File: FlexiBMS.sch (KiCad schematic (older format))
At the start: 6 parts, among them J1 Conn_02x08_Odd_Even, J7 Conn_01x03

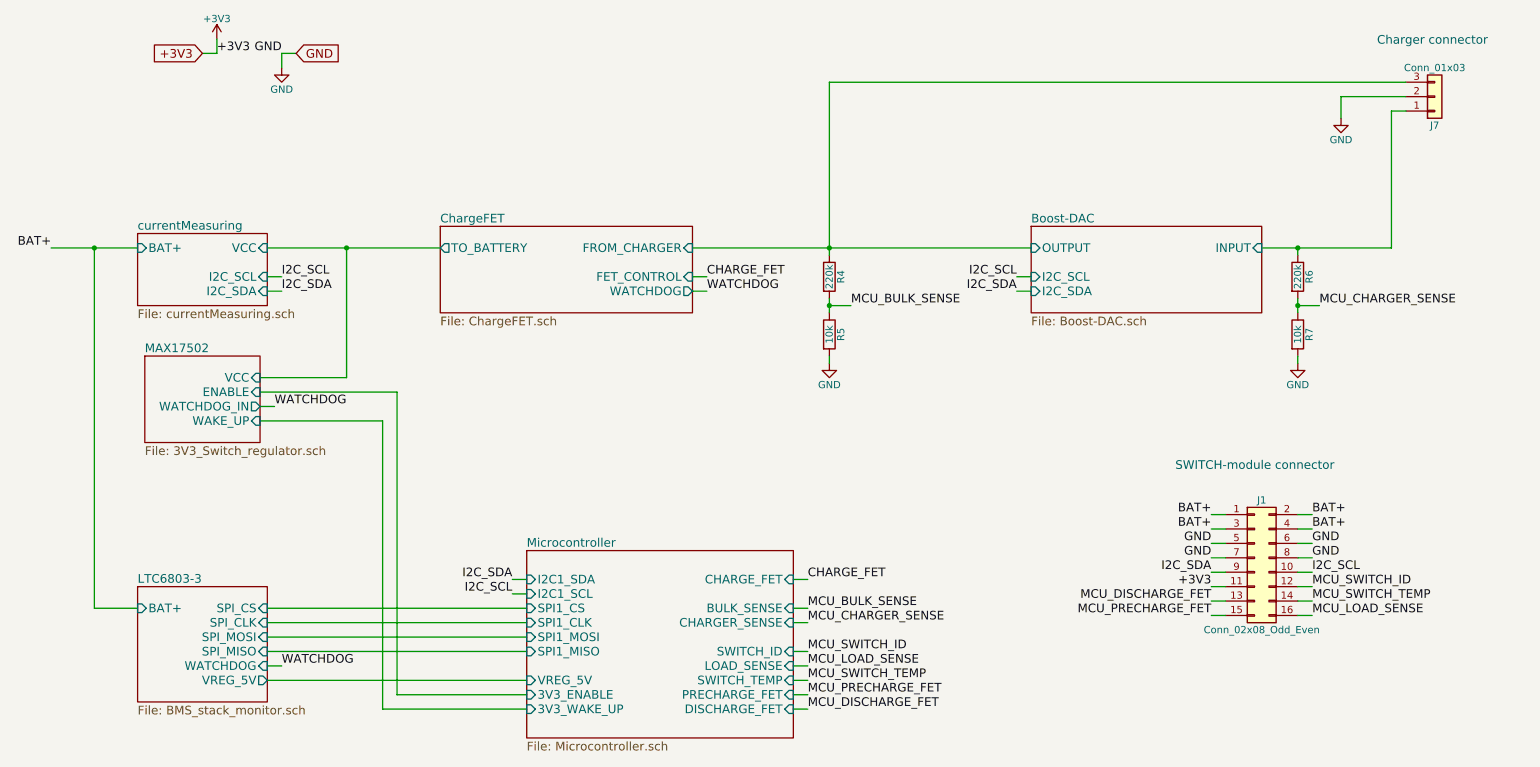
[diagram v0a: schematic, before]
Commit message: HW 0.2 finalized schematic and pcb files, BOM needs to be checked
Lots of major and little problems fixed found in the 0.1

Major changes:
-LTC6803-3 footprint changed to it's correct one
-Boost converter layout and capacitor optimization
-MCU switched from STM32F070CBT6 to ultra low power STM32L433CCT6 to improve sleep state power consumption
-Button/LED + Comms connectors switched from THT JST-XH to SMD JST-PH
-CAN-bus support added
-Changed power regulator setup for "always on"

Minor changes:
-Changed cell balance resistor sizes from 0603 to 0402 in order to get a bit more breathing room during soldering
-External oscillator removed from MCU, because new one has everything available internally
-Comms connector has USART or CAN available via solder bridges
-Sense resistors switched to higher resistance ones to lower deep sleep standby current
-etc.
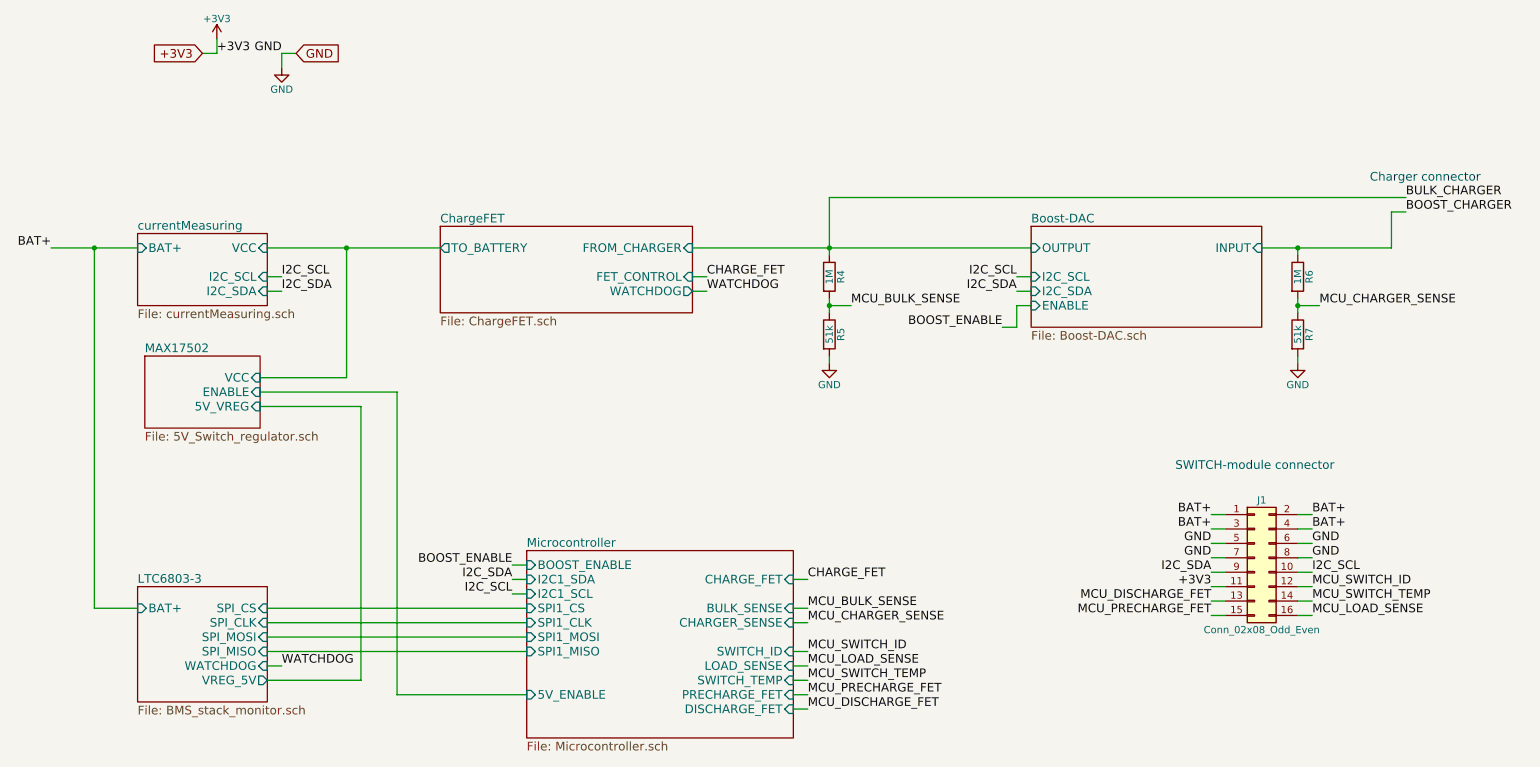
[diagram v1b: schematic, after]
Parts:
- removed J7: Conn_01x03, Connectors_Phoenix:PhoenixContact_MCV-G_03x3.50mm_Vertical, symbol Conn_01x03
- J1: MFG PREC008DAAN-RC -> \"PREC008DAAN-RC\"/\"PPTC082LFBN-RC\"/\"SFH210-PPPC-D08-ID-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
- R4, R6: value 220k -> 1M; MFG RC0603FR-07220KL -> ANY; Tol. (none) -> 1%
- R5, R7: value 10k -> 51k; MFG RC0603FR-0710KL -> ANY; Tol. (none) -> 1%
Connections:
- net Boost-DAC/INPUT renamed BOOST_CHARGER
- net Boost-DAC/OUTPUT renamed BULK_CHARGER
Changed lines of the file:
@@
 LIBS:valves
 LIBS:Custom_comp_lib
-LIBS:FlexiBMS_01-cache
+LIBS:FlexiBMS-cache
 EELAYER 25 0
 EELAYER END
@@
 Title "FlexiBMS"
 Date "2018-02-22"
-Rev "0.1"
+Rev "0.2"
 Comp "SiMoS MCmuffin / Simo Sihvonen"
 Comment1 ""
@@
 F14 "DISCHARGE_FET" I R 6150 5850 60
 F15 "CHARGE_FET" I R 6150 4950 60
-F16 "VREG_5V" I L 4300 5650 60
-F17 "3V3_ENABLE" I L 4300 5750 60
-F18 "3V3_WAKE_UP" I L 4300 5850 60
+F16 "5V_ENABLE" I L 4300 5750 60
+F17 "BOOST_ENABLE" I L 4300 4850 60
 $EndSheet
 $Sheet
@@
 $EndSheet
 $Sheet
-S 1650 3400 800  600
+S 1650 3400 800  500
 U 5A8293EE
 F0 "MAX17502" 60
-F1 "3V3_Switch_regulator.sch" 60
+F1 "5V_Switch_regulator.sch" 60
 F2 "VCC" I R 2450 3550 60
 F3 "ENABLE" I R 2450 3650 60
-F4 "WATCHDOG_IN" O R 2450 3750 60
-F5 "WAKE_UP" I R 2450 3850 60
+F4 "5V_VREG" I R 2450 3750 60
 $EndSheet
 $Sheet
@@
 $EndSheet
 $Sheet
-S 7800 2500 1600 600
+S 7800 2500 1600 700
 U 5A830810
 F0 "Boost-DAC" 60
@@
 F4 "OUTPUT" I L 7800 2650 60
 F5 "INPUT" I R 9400 2650 60
+F6 "ENABLE" I L 7800 3050 60
 $EndSheet
 Text Label 1000 2650 2    60   ~ 0
@@
 F 2 "Pin_Headers:Pin_Header_Straight_2x08_Pitch2.54mm" H 9350 4800 50  0001 C CNN
 F 3 "" H 9350 4800 50  0001 C CNN
-F 4 "PREC008DAAN-RC" H 9350 4800 60  0001 C CNN "MFG"
+F 4 "\"PREC008DAAN-RC\"/\"PPTC082LFBN-RC\"/\"SFH210-PPPC-D08-ID-BK\"" H 9350 4800 60  0001 C CNN "MFG"
 	1    9350 4800
 	1    0    0    -1
@@
 P 9650 2850
 F 0 "R6" V 9730 2850 50  0000 C CNN
-F 1 "220k" V 9650 2850 50  0000 C CNN
+F 1 "1M" V 9650 2850 50  0000 C CNN
 F 2 "Resistors_SMD:R_0603" V 9580 2850 50  0001 C CNN
 F 3 "" H 9650 2850 50  0001 C CNN
-F 4 "RC0603FR-07220KL" V 9650 2850 60  0001 C CNN "MFG"
+F 4 "ANY" V 9650 2850 60  0001 C CNN "MFG"
+F 5 "1%" V 9650 2850 60  0001 C CNN "Tol."
 	1    9650 2850
 	1    0    0    -1
@@
 P 9650 3250
 F 0 "R7" V 9730 3250 50  0000 C CNN
-F 1 "10k" V 9650 3250 50  0000 C CNN
+F 1 "51k" V 9650 3250 50  0000 C CNN
 F 2 "Resistors_SMD:R_0603" V 9580 3250 50  0001 C CNN
 F 3 "" H 9650 3250 50  0001 C CNN
-F 4 "RC0603FR-0710KL" V 9650 3250 60  0001 C CNN "MFG"
+F 4 "ANY" V 9650 3250 60  0001 C CNN "MFG"
+F 5 "1%" V 9650 3250 60  0001 C CNN "Tol."
 	1    9650 3250
 	1    0    0    -1
@@
 P 6400 2850
 F 0 "R4" V 6480 2850 50  0000 C CNN
-F 1 "220k" V 6400 2850 50  0000 C CNN
+F 1 "1M" V 6400 2850 50  0000 C CNN
 F 2 "Resistors_SMD:R_0603" V 6330 2850 50  0001 C CNN
 F 3 "" H 6400 2850 50  0001 C CNN
-F 4 "RC0603FR-07220KL" V 6400 2850 60  0001 C CNN "MFG"
+F 4 "ANY" V 6400 2850 60  0001 C CNN "MFG"
+F 5 "1%" V 6400 2850 60  0001 C CNN "Tol."
 	1    6400 2850
 	1    0    0    -1
@@
 P 6400 3250
 F 0 "R5" V 6480 3250 50  0000 C CNN
-F 1 "10k" V 6400 3250 50  0000 C CNN
+F 1 "51k" V 6400 3250 50  0000 C CNN
 F 2 "Resistors_SMD:R_0603" V 6330 3250 50  0001 C CNN
 F 3 "" H 6400 3250 50  0001 C CNN
-F 4 "RC0603FR-0710KL" V 6400 3250 60  0001 C CNN "MFG"
+F 4 "ANY" V 6400 3250 60  0001 C CNN "MFG"
+F 5 "1%" V 6400 3250 60  0001 C CNN "Tol."
 	1    6400 3250
 	1    0    0    -1
@@
 Text GLabel 2700 1300 2    60   Input ~ 0
 GND
-$Comp
-L Conn_01x03 J7
-U 1 1 5A841E1F
-P 10600 1600
-F 0 "J7" H 10600 1800 50  0000 C CNN
-F 1 "Conn_01x03" H 10600 1400 50  0000 C CNN
-F 2 "Connectors_Phoenix:PhoenixContact_MCV-G_03x3.50mm_Vertical" H 10600 1600 50  0001 C CNN
-F 3 "" H 10600 1600 50  0001 C CNN
-F 4 "OSTTE030104" H 10600 1600 60  0001 C CNN "MFG"
-	1    10600 1600
-	1    0    0    1
-$EndComp
-$Comp
-L GND #PWR05
-U 1 1 5A842621
-P 9950 1750
-F 0 "#PWR05" H 9950 1500 50  0001 C CNN
-F 1 "GND" H 9950 1600 50  0000 C CNN
-F 2 "" H 9950 1750 50  0001 C CNN
-F 3 "" H 9950 1750 50  0001 C CNN
-	1    9950 1750
-	1    0    0    -1
-$EndComp
 Text Label 2600 5550 0    60   ~ 0
 WATCHDOG
@@
 	6400 3400 6400 3450
 Wire Wire Line
-	6400 1500 6400 2700
+	6400 2300 6400 2700
 Connection ~ 6400 2650
 Wire Wire Line
-	10400 1600 9950 1600
-Wire Wire Line
-	9950 1600 9950 1750
-Wire Wire Line
-	10400 1700 10300 1700
-Wire Wire Line
-	10300 1700 10300 2650
-Wire Wire Line
-	10400 1500 6400 1500
+	10400 2400 10300 2400
+Wire Wire Line
+	10300 2400 10300 2650
+Wire Wire Line
+	10400 2300 6400 2300
 Wire Wire Line
 	7700 2850 7800 2850
@@
 	2500 5550 2600 5550
 Text Label 5550 2950 0    60   ~ 0
-WATCHDOG
-Text Label 2550 3750 0    60   ~ 0
 WATCHDOG
 Wire Wire Line
@@
 Wire Wire Line
 	2450 3650 3400 3650
-Wire Wire Line
-	2550 3750 2450 3750
-Text Notes 10200 1250 0    60   ~ 0
+Text Notes 10150 2200 0    60   ~ 0
 Charger connector
 Wire Wire Line
-	2500 5650 4300 5650
-Wire Wire Line
-	2450 3850 3300 3850
-Wire Wire Line
 	3400 5750 4300 5750
 Wire Wire Line
-	3300 5850 4300 5850
-Wire Wire Line
 	3400 3650 3400 5750
 Wire Wire Line
-	3300 3850 3300 5850
+	2500 5650 3150 5650
+Wire Wire Line
+	3150 5650 3150 3750
+Wire Wire Line
+	3150 3750 2450 3750
+Text Label 10400 2300 0    60   ~ 0
+BULK_CHARGER
+Text Label 10400 2400 0    60   ~ 0
+BOOST_CHARGER
+Wire Wire Line
+	7800 3050 7700 3050
+Text Label 7600 3200 2    60   ~ 0
+BOOST_ENABLE
+Wire Wire Line
+	7700 3050 7700 3200
+Wire Wire Line
+	7700 3200 7600 3200
+Wire Wire Line
+	4300 4850 4200 4850
+Text Label 4200 4850 2    60   ~ 0
+BOOST_ENABLE
 $EndSCHEMATC
